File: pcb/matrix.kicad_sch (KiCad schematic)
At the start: 177 parts, among them SW10 Tab, SW11 CapsLock, SW12 Shift, SW13 Ctrl, SW14 F1, SW15 1, SW16 Q, SW17 A, SW18 Z, SW19 Win, SW20 F2, SW21 2, SW22 W, SW23 S, SW24 X, SW25 F3, SW26 3, SW27 E, SW28 D, SW29 C, SW30 F4, SW31 4, SW32 R, SW33 F, SW34 V, SW35 F5, SW36 5, SW37 T, SW38 G, SW39 B, SW4 M1, SW40 Space, SW41 F6, SW42 6, SW43 Y, SW44 H, SW45 N, SW46 F7, SW47 7, SW48 U, SW49 J, SW5 M2, SW50 M, SW51 F8, SW52 8, SW53 I, SW54 K, SW55 Comma, SW56 RAlt, SW57 F9, SW58 9, SW59 O, SW6 M3, SW60 L, SW61 Period, SW62 RFn, SW63 F10, SW64 0, SW65 P, SW66 Semicolon, SW67 Slash, SW68 RCtrl, SW69 F11, SW7 M4, SW70 Minus, SW71 LBrkt, SW72 Quote, SW73 RShift, SW74 F12, SW75 Equals, SW76 RBrkt, SW77 Enter, SW78 LArr, SW79 F13, SW8 Esc, SW80 Bksp, SW81 Bkslash, SW82 UArr, SW83 DArr, SW84 Knob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

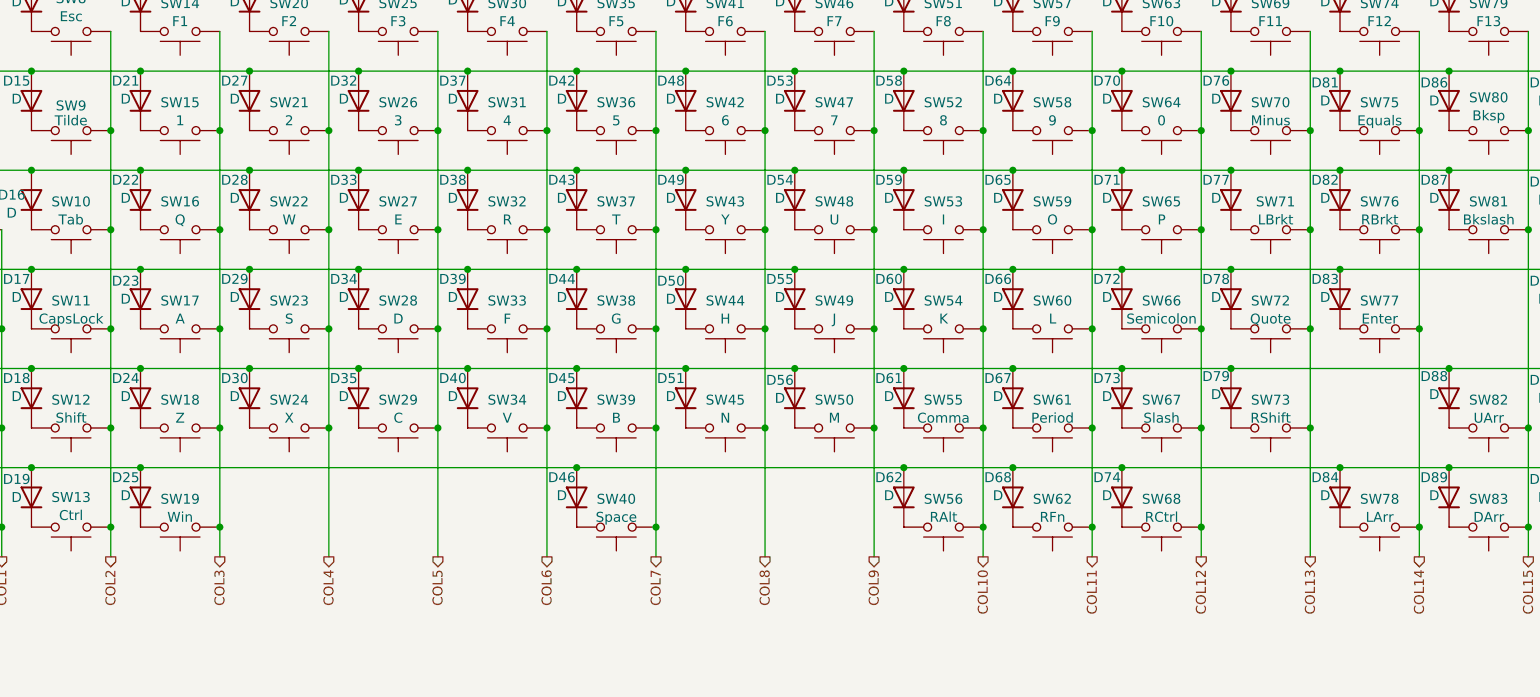
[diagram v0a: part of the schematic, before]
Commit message: Add keyboard layout to pcb layout
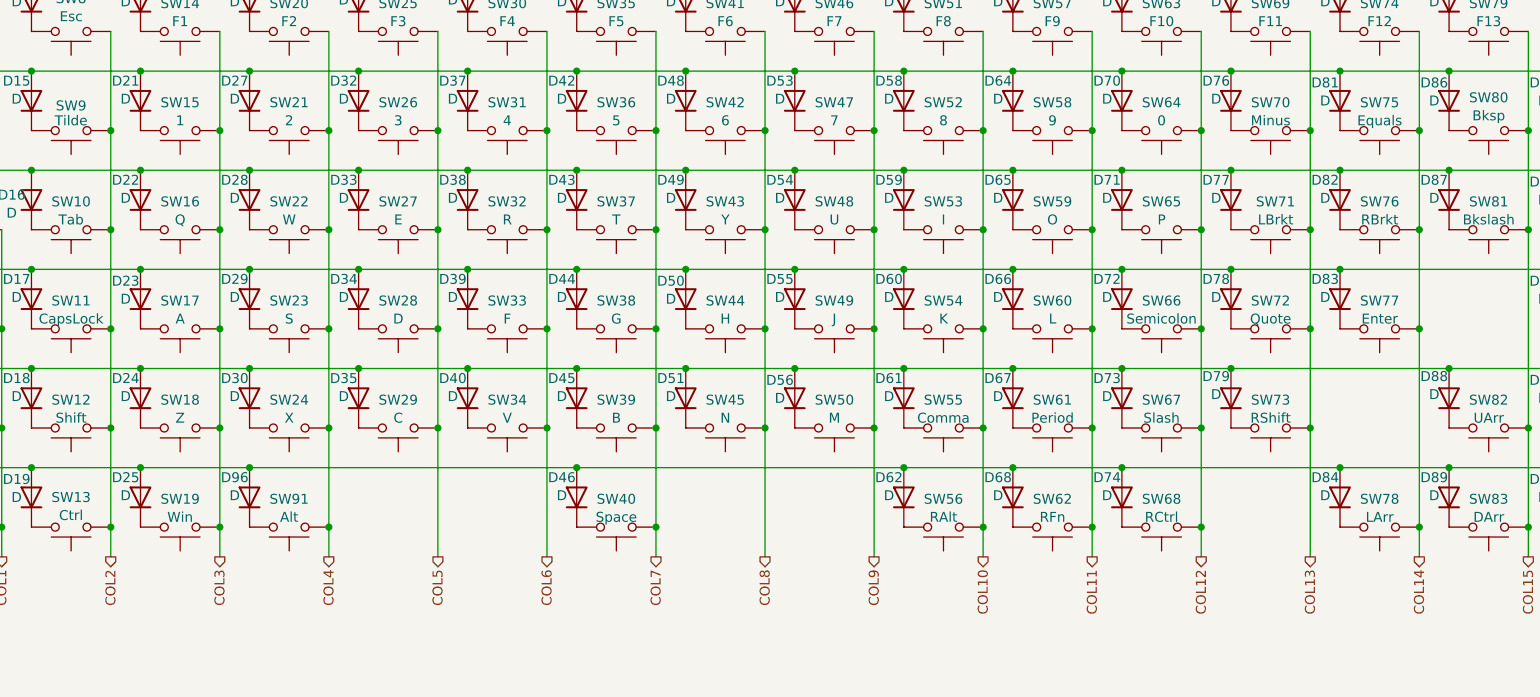
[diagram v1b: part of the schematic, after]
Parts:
- added D96: D, Diode_SMD:D_SOD-323, symbol Device:D
- added SW91: Alt, Switch_Keyboard_Kailh:SW_Hotswap_Kailh_MX_plated_1.25u, symbol Switch:SW_Push
- SW10, SW11, SW12, SW14, SW15, SW16, SW17, SW18, SW20, SW21, SW22, SW23, SW24, SW25, SW26, SW27, SW28, SW29, SW30, SW31, SW32, SW33, SW34, SW35, SW36, SW37, SW38, SW39, SW41, SW42, SW43, SW44, SW45, SW46, SW47, SW48, SW49, SW50, SW51, SW52, SW53, SW54, SW55, SW57, SW58, SW59, SW60, SW61, SW63, SW64, SW65, SW66, SW67, SW69, SW70, SW71, SW74, SW76, SW77, SW78, SW79, SW8, SW82, SW83, SW84, SW85, SW86, SW87, SW88, SW89, SW9: footprint Switch_Keyboard_Kailh:SW_Hotswap_Kailh_1.00u -> Switch_Keyboard_Kailh:SW_Hotswap_Kailh_MX_plated_1.00u
- SW13, SW19, SW56, SW62, SW68, SW7, SW72: footprint Switch_Keyboard_Kailh:SW_Hotswap_Kailh_1.25u -> Switch_Keyboard_Kailh:SW_Hotswap_Kailh_MX_plated_1.25u
- SW4: footprint Switch_Keyboard_Kailh:SW_Hotswap_Kailh_1.50u -> Switch_Keyboard_Kailh:SW_Hotswap_Kailh_MX_plated_1.50u
- SW40: footprint Switch_Keyboard_Kailh:SW_Hotswap_Kailh_2.25u -> Switch_Keyboard_Kailh:SW_Hotswap_Kailh_MX_plated_6.25u
- SW5: footprint Switch_Keyboard_Kailh:SW_Hotswap_Kailh_1.75u_SteppedCapsLock -> Switch_Keyboard_Kailh:SW_Hotswap_Kailh_MX_1.75u_SteppedCapsLock
- SW6: footprint Switch_Keyboard_Kailh:SW_Hotswap_Kailh_2.25u -> Switch_Keyboard_Kailh:SW_Hotswap_Kailh_MX_plated_2.25u
- SW73: footprint Switch_Keyboard_Kailh:SW_Hotswap_Kailh_1.75u -> Switch_Keyboard_Kailh:SW_Hotswap_Kailh_MX_plated_1.75u
- SW75: footprint Switch_Keyboard_Kailh:SW_Hotswap_Kailh_2.00u -> Switch_Keyboard_Kailh:SW_Hotswap_Kailh_MX_1.00u
- SW80: footprint Switch_Keyboard_Kailh:SW_Hotswap_Kailh_1.00u -> Switch_Keyboard_Kailh:SW_Hotswap_Kailh_MX_plated_2.00u
- SW81: footprint Switch_Keyboard_Kailh:SW_Hotswap_Kailh_1.00u -> Switch_Keyboard_Kailh:SW_Hotswap_Kailh_MX_plated_1.50u
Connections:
- net COL14: now also SW75.2; no longer SW75.1
- net COL4: now also SW91.1
- net ROW6: now also D96.2 (A)
- net at D81.1 (K): now also SW75.1; no longer SW75.2
- new net: D96.1 (K), SW91.2
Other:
- moved on the sheet: SW75

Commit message: Arrange the rest of the switches
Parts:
- SW10: footprint Switch_Keyboard_Kailh:SW_Hotswap_Kailh_MX_plated_1.00u -> Switch_Keyboard_Kailh:SW_Hotswap_Kailh_MX_plated_1.50u
- SW11: footprint Switch_Keyboard_Kailh:SW_Hotswap_Kailh_MX_plated_1.00u -> Switch_Keyboard_Kailh:SW_Hotswap_Kailh_MX_1.75u_SteppedCapsLock
- SW12, SW77: footprint Switch_Keyboard_Kailh:SW_Hotswap_Kailh_MX_plated_1.00u -> Switch_Keyboard_Kailh:SW_Hotswap_Kailh_MX_plated_2.25u
- SW4: footprint Switch_Keyboard_Kailh:SW_Hotswap_Kailh_MX_plated_1.50u -> Switch_Keyboard_Kailh:SW_Hotswap_Kailh_MX_plated_1.00u
- SW5: footprint Switch_Keyboard_Kailh:SW_Hotswap_Kailh_MX_1.75u_SteppedCapsLock -> Switch_Keyboard_Kailh:SW_Hotswap_Kailh_MX_plated_1.00u
- SW56, SW62, SW68, SW7, SW72: footprint Switch_Keyboard_Kailh:SW_Hotswap_Kailh_MX_plated_1.25u -> Switch_Keyboard_Kailh:SW_Hotswap_Kailh_MX_plated_1.00u
- SW6: footprint Switch_Keyboard_Kailh:SW_Hotswap_Kailh_MX_plated_2.25u -> Switch_Keyboard_Kailh:SW_Hotswap_Kailh_MX_plated_1.00u
- SW75: footprint Switch_Keyboard_Kailh:SW_Hotswap_Kailh_MX_1.00u -> Switch_Keyboard_Kailh:SW_Hotswap_Kailh_MX_plated_1.00u
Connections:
- net COL14: now also SW75.1; no longer SW75.2
- net at D81.1 (K): now also SW75.2; no longer SW75.1
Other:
- moved on the sheet: SW75
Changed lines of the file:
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@@
   (junction (at 232.41 132.08) (diameter 0) (color 0 0 0 0)
   )
+  (junction (at 228.6 88.9) (diameter 0) (color 0 0 0 0)
+  )
   (junction (at 116.84 88.9) (diameter 0) (color 0 0 0 0)
   )
@@
   (junction (at 36.83 119.38) (diameter 0) (color 0 0 0 0)
   )
-  (junction (at 228.6 88.9) (diameter 0) (color 0 0 0 0)
-  )
   (junction (at 78.74 106.68) (diameter 0) (color 0 0 0 0)
   )
@@
     (stroke (width 0) (type default) (color 0 0 0 0))
   )
+  (wire (pts (xy 228.6 88.9) (xy 228.6 101.6))
+    (stroke (width 0) (type default) (color 0 0 0 0))
+  )
   (wire (pts (xy 176.53 106.68) (xy 190.5 106.68))
     (stroke (width 0) (type default) (color 0 0 0 0))
@@
     (stroke (width 0) (type default) (color 0 0 0 0))
   )
+  (wire (pts (xy 218.44 93.98) (xy 232.41 93.98))
+    (stroke (width 0) (type default) (color 0 0 0 0))
+  )
   (wire (pts (xy 204.47 81.28) (xy 218.44 81.28))
     (stroke (width 0) (type default) (color 0 0 0 0))
@@
     (stroke (width 0) (type default) (color 0 0 0 0))
   )
-  (wire (pts (xy 228.6 76.2) (xy 228.6 88.9))
-    (stroke (width 0) (type default) (color 0 0 0 0))
-  )
   (wire (pts (xy 130.81 139.7) (xy 130.81 143.51))
     (stroke (width 0) (type default) (color 0 0 0 0))
@@
     (stroke (width 0) (type default) (color 0 0 0 0))
   )
-  (wire (pts (xy 218.44 93.98) (xy 232.41 93.98))
-    (stroke (width 0) (type default) (color 0 0 0 0))
-  )
   (wire (pts (xy 130.81 114.3) (xy 130.81 127))
     (stroke (width 0) (type default) (color 0 0 0 0))
@@
     (stroke (width 0) (type default) (color 0 0 0 0))
   )
+  (wire (pts (xy 228.6 76.2) (xy 228.6 88.9))
+    (stroke (width 0) (type default) (color 0 0 0 0))
+  )
   (wire (pts (xy 190.5 93.98) (xy 204.47 93.98))
     (stroke (width 0) (type default) (color 0 0 0 0))
@@
     (stroke (width 0) (type default) (color 0 0 0 0))
   )
-  (wire (pts (xy 228.6 88.9) (xy 228.6 101.6))
-    (stroke (width 0) (type default) (color 0 0 0 0))
-  )
   (wire (pts (xy 78.74 119.38) (xy 92.71 119.38))
     (stroke (width 0) (type default) (color 0 0 0 0))
@@
     (property "Reference" "SW62" (id 0) (at 181.61 136.1186 0))
     (property "Value" "RFn" (id 1) (at 181.61 138.43 0))
-    (property "Footprint" "Switch_Keyboard_Kailh:SW_Hotswap_Kailh_MX_plated_1.25u" (id 2) (at 181.61 144.78 0)
+    (property "Footprint" "Switch_Keyboard_Kailh:SW_Hotswap_Kailh_MX_plated_1.00u" (id 2) (at 181.61 144.78 0)
       (effects (font (size 1.27 1.27)) hide)
     )
@@
     (pin "2")
   )
-  (symbol (lib_id "Switch:SW_Push") (at 223.52 88.9 0) (mirror x) (unit 1)
+  (symbol (lib_id "Switch:SW_Push") (at 223.52 88.9 180) (unit 1)
     (in_bom yes) (on_board yes)
     (property "Reference" "SW75" (id 0) (at 223.52 85.3186 0))
     (property "Value" "Equals" (id 1) (at 223.52 87.63 0))
-    (property "Footprint" "Switch_Keyboard_Kailh:SW_Hotswap_Kailh_MX_1.00u" (id 2) (at 223.52 93.98 0)
+    (property "Footprint" "Switch_Keyboard_Kailh:SW_Hotswap_Kailh_MX_plated_1.00u" (id 2) (at 223.52 93.98 0)
       (effects (font (size 1.27 1.27)) hide)
     )
@@
     (property "Reference" "SW12" (id 0) (at 55.88 123.4186 0))
     (property "Value" "Shift" (id 1) (at 55.88 125.73 0))
-    (property "Footprint" "Switch_Keyboard_Kailh:SW_Hotswap_Kailh_MX_plated_1.00u" (id 2) (at 55.88 132.08 0)
+    (property "Footprint" "Switch_Keyboard_Kailh:SW_Hotswap_Kailh_MX_plated_2.25u" (id 2) (at 55.88 132.08 0)
       (effects (font (size 1.27 1.27)) hide)
     )
@@
     (property "Reference" "SW77" (id 0) (at 223.52 110.7186 0))
     (property "Value" "Enter" (id 1) (at 223.52 113.03 0))
-    (property "Footprint" "Switch_Keyboard_Kailh:SW_Hotswap_Kailh_MX_plated_1.00u" (id 2) (at 223.52 119.38 0)
+    (property "Footprint" "Switch_Keyboard_Kailh:SW_Hotswap_Kailh_MX_plated_2.25u" (id 2) (at 223.52 119.38 0)
       (effects (font (size 1.27 1.27)) hide)
     )
@@
     (property "Reference" "SW11" (id 0) (at 55.88 110.7186 0))
     (property "Value" "CapsLock" (id 1) (at 55.88 113.03 0))
-    (property "Footprint" "Switch_Keyboard_Kailh:SW_Hotswap_Kailh_MX_plated_1.00u" (id 2) (at 55.88 119.38 0)
+    (property "Footprint" "Switch_Keyboard_Kailh:SW_Hotswap_Kailh_MX_1.75u_SteppedCapsLock" (id 2) (at 55.88 119.38 0)
       (effects (font (size 1.27 1.27)) hide)
     )
@@
     (property "Reference" "SW56" (id 0) (at 167.64 136.1186 0))
     (property "Value" "RAlt" (id 1) (at 167.64 138.43 0))
-    (property "Footprint" "Switch_Keyboard_Kailh:SW_Hotswap_Kailh_MX_plated_1.25u" (id 2) (at 167.64 144.78 0)
+    (property "Footprint" "Switch_Keyboard_Kailh:SW_Hotswap_Kailh_MX_plated_1.00u" (id 2) (at 167.64 144.78 0)
       (effects (font (size 1.27 1.27)) hide)
     )
@@
     (property "Reference" "SW4" (id 0) (at 41.91 98.0186 0))
     (property "Value" "M1" (id 1) (at 41.91 100.33 0))
-    (property "Footprint" "Switch_Keyboard_Kailh:SW_Hotswap_Kailh_MX_plated_1.50u" (id 2) (at 41.91 106.68 0)
+    (property "Footprint" "Switch_Keyboard_Kailh:SW_Hotswap_Kailh_MX_plated_1.00u" (id 2) (at 41.91 106.68 0)
       (effects (font (size 1.27 1.27)) hide)
     )
@@
     (property "Reference" "SW72" (id 0) (at 209.55 110.7186 0))
     (property "Value" "Quote" (id 1) (at 209.55 113.03 0))
-    (property "Footprint" "Switch_Keyboard_Kailh:SW_Hotswap_Kailh_MX_plated_1.25u" (id 2) (at 209.55 119.38 0)
+    (property "Footprint" "Switch_Keyboard_Kailh:SW_Hotswap_Kailh_MX_plated_1.00u" (id 2) (at 209.55 119.38 0)
       (effects (font (size 1.27 1.27)) hide)
     )
@@
     (property "Reference" "SW6" (id 0) (at 41.91 123.4186 0))
     (property "Value" "M3" (id 1) (at 41.91 125.73 0))
-    (property "Footprint" "Switch_Keyboard_Kailh:SW_Hotswap_Kailh_MX_plated_2.25u" (id 2) (at 41.91 132.08 0)
+    (property "Footprint" "Switch_Keyboard_Kailh:SW_Hotswap_Kailh_MX_plated_1.00u" (id 2) (at 41.91 132.08 0)
       (effects (font (size 1.27 1.27)) hide)
     )
@@
     (property "Reference" "SW68" (id 0) (at 195.58 136.1186 0))
     (property "Value" "RCtrl" (id 1) (at 195.58 138.43 0))
-    (property "Footprint" "Switch_Keyboard_Kailh:SW_Hotswap_Kailh_MX_plated_1.25u" (id 2) (at 195.58 144.78 0)
+    (property "Footprint" "Switch_Keyboard_Kailh:SW_Hotswap_Kailh_MX_plated_1.00u" (id 2) (at 195.58 144.78 0)
       (effects (font (size 1.27 1.27)) hide)
     )
@@
     (property "Reference" "SW7" (id 0) (at 41.91 136.1186 0))
     (property "Value" "M4" (id 1) (at 41.91 138.43 0))
-    (property "Footprint" "Switch_Keyboard_Kailh:SW_Hotswap_Kailh_MX_plated_1.25u" (id 2) (at 41.91 144.78 0)
+    (property "Footprint" "Switch_Keyboard_Kailh:SW_Hotswap_Kailh_MX_plated_1.00u" (id 2) (at 41.91 144.78 0)
       (effects (font (size 1.27 1.27)) hide)
     )
@@
     (property "Reference" "SW10" (id 0) (at 55.88 98.0186 0))
     (property "Value" "Tab" (id 1) (at 55.88 100.33 0))
-    (property "Footprint" "Switch_Keyboard_Kailh:SW_Hotswap_Kailh_MX_plated_1.00u" (id 2) (at 55.88 106.68 0)
+    (property "Footprint" "Switch_Keyboard_Kailh:SW_Hotswap_Kailh_MX_plated_1.50u" (id 2) (at 55.88 106.68 0)
       (effects (font (size 1.27 1.27)) hide)
     )
@@
     (property "Reference" "SW5" (id 0) (at 41.91 110.7186 0))
     (property "Value" "M2" (id 1) (at 41.91 113.03 0))
-    (property "Footprint" "Switch_Keyboard_Kailh:SW_Hotswap_Kailh_MX_1.75u_SteppedCapsLock" (id 2) (at 41.91 119.38 0)
+    (property "Footprint" "Switch_Keyboard_Kailh:SW_Hotswap_Kailh_MX_plated_1.00u" (id 2) (at 41.91 119.38 0)
       (effects (font (size 1.27 1.27)) hide)
     )
